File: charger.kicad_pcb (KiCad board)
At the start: 2 copper layers, 3 parts, among them J2 USB_C_Receptacle_PowerOnly_6P

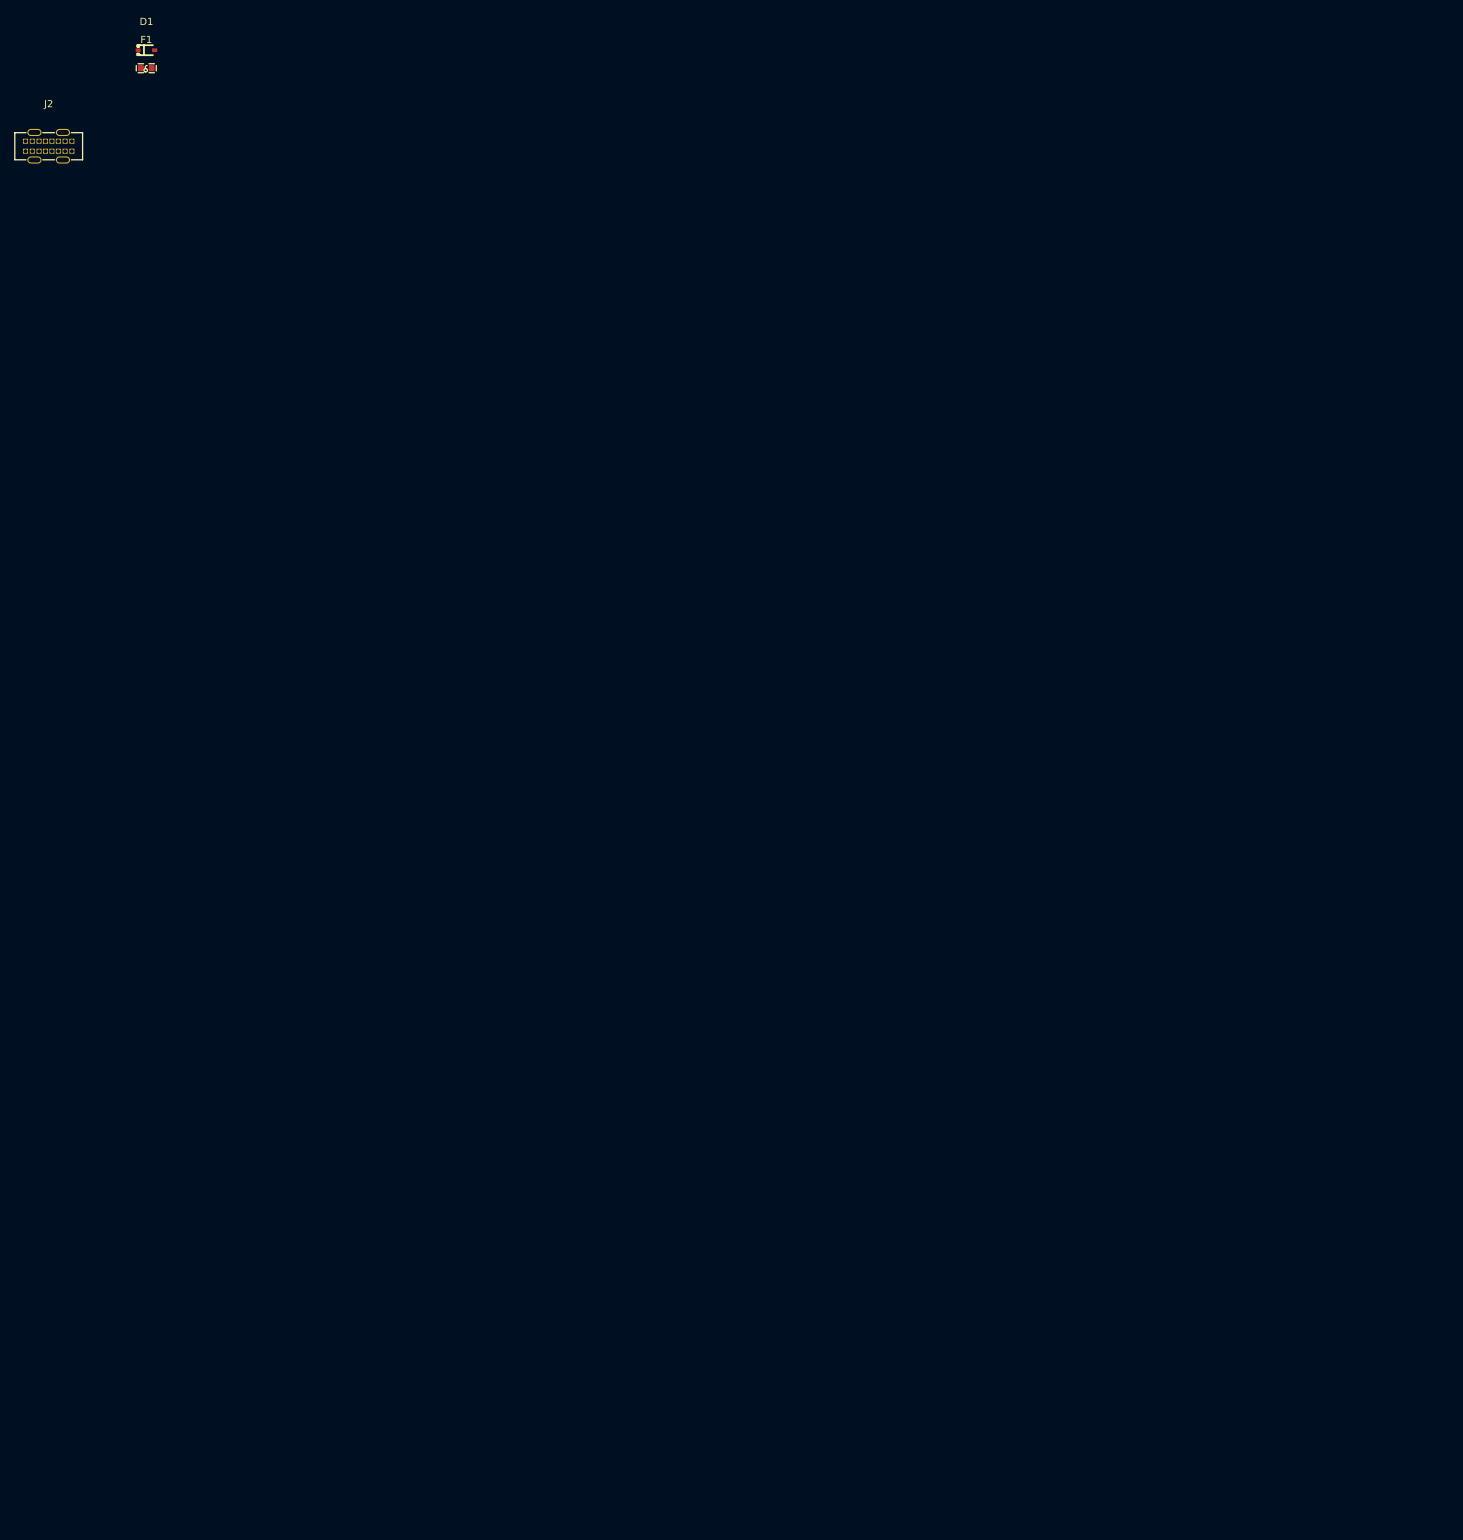
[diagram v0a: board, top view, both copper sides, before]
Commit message: finished getting footprints and started layout
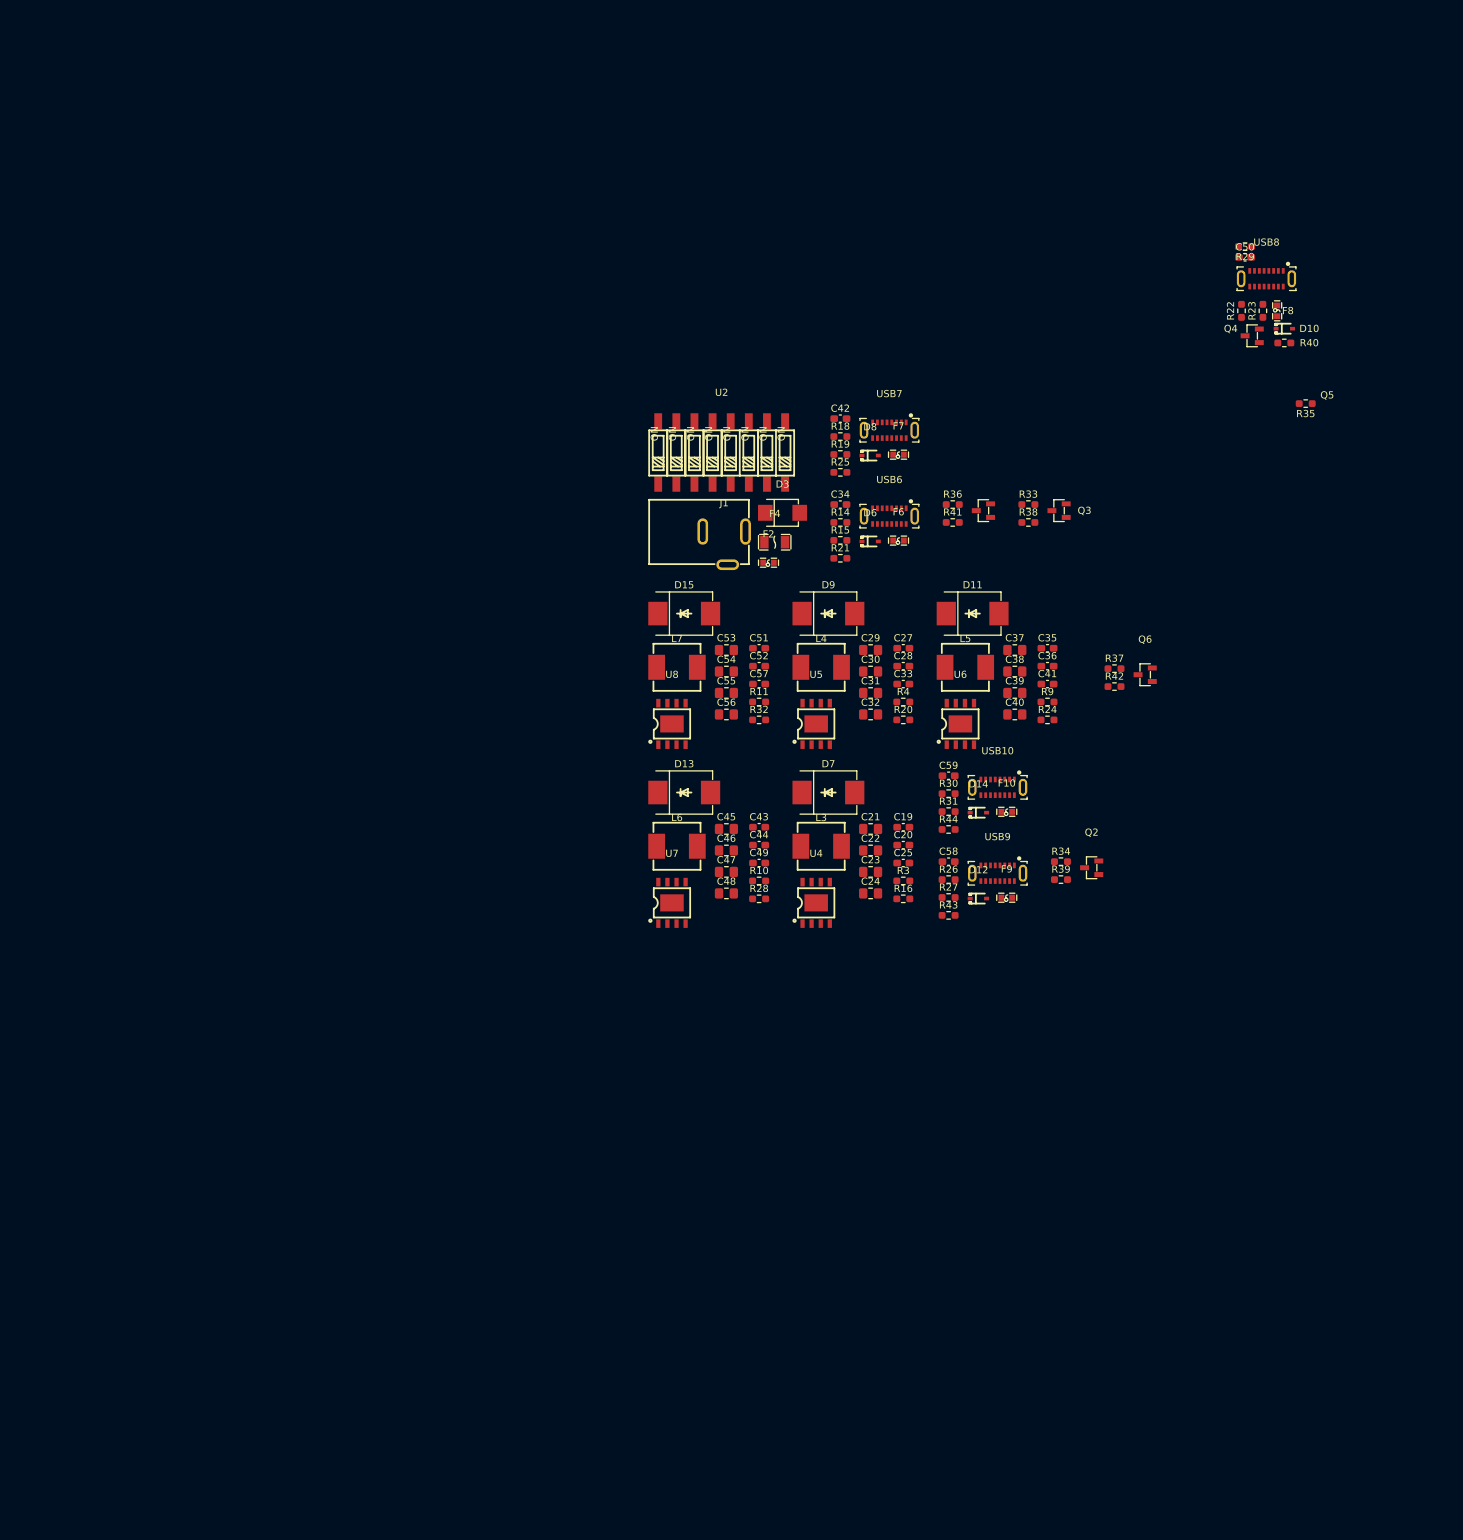
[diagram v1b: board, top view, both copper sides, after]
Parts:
- removed D1: DF2S6P2FU,H3F, easyeda2kicad:USC_L1.7-W1.3-LS2.5-R-RD
- removed F1: Fuse, easyeda2kicad:F0603
- removed J2: USB_C_Receptacle_PowerOnly_6P, easyeda2kicad:TYPE-C-TH_16PLC-H10.0
- added C19: 10nf, Capacitor_SMD:C_0603_1608Metric_Pad1.08x0.95mm_HandSolder, F.Cu at (124.6, 97.9)
- added C20: 0.1uf, Capacitor_SMD:C_0603_1608Metric_Pad1.08x0.95mm_HandSolder, F.Cu at (124.6, 100.4)
- added C21: 10uf, Capacitor_SMD:C_0805_2012Metric_Pad1.18x1.45mm_HandSolder, F.Cu at (120.0, 98.1)
- added C22: 22uF, Capacitor_SMD:C_0805_2012Metric_Pad1.18x1.45mm_HandSolder, F.Cu at (120.0, 101.1)
- added C23: 22uF, Capacitor_SMD:C_0805_2012Metric_Pad1.18x1.45mm_HandSolder, F.Cu at (120.0, 104.1)
- added C24: 10uf, Capacitor_SMD:C_0805_2012Metric_Pad1.18x1.45mm_HandSolder, F.Cu at (120.0, 107.2)
- added C25: 0.1uf, Capacitor_SMD:C_0603_1608Metric_Pad1.08x0.95mm_HandSolder, F.Cu at (124.6, 102.9)
- added C27: 10nf, Capacitor_SMD:C_0603_1608Metric_Pad1.08x0.95mm_HandSolder, F.Cu at (124.6, 72.8)
- added C28: 0.1uf, Capacitor_SMD:C_0603_1608Metric_Pad1.08x0.95mm_HandSolder, F.Cu at (124.6, 75.3)
- added C29: 10uf, Capacitor_SMD:C_0805_2012Metric_Pad1.18x1.45mm_HandSolder, F.Cu at (120.0, 73.0)
- added C30: 22uF, Capacitor_SMD:C_0805_2012Metric_Pad1.18x1.45mm_HandSolder, F.Cu at (120.0, 76.0)
- added C31: 22uF, Capacitor_SMD:C_0805_2012Metric_Pad1.18x1.45mm_HandSolder, F.Cu at (120.0, 79.1)
- added C32: 10uf, Capacitor_SMD:C_0805_2012Metric_Pad1.18x1.45mm_HandSolder, F.Cu at (120.0, 82.1)
- added C33: 0.1uf, Capacitor_SMD:C_0603_1608Metric_Pad1.08x0.95mm_HandSolder, F.Cu at (124.6, 77.8)
- added C34: 4n7, Capacitor_SMD:C_0603_1608Metric_Pad1.08x0.95mm_HandSolder, F.Cu at (115.8, 52.6)
- added C35: 10nf, Capacitor_SMD:C_0603_1608Metric_Pad1.08x0.95mm_HandSolder, F.Cu at (144.8, 72.8)
- added C36: 0.1uf, Capacitor_SMD:C_0603_1608Metric_Pad1.08x0.95mm_HandSolder, F.Cu at (144.8, 75.3)
- added C37: 10uf, Capacitor_SMD:C_0805_2012Metric_Pad1.18x1.45mm_HandSolder, F.Cu at (140.2, 73.0)
- added C38: 22uF, Capacitor_SMD:C_0805_2012Metric_Pad1.18x1.45mm_HandSolder, F.Cu at (140.2, 76.0)
- added C39: 22uF, Capacitor_SMD:C_0805_2012Metric_Pad1.18x1.45mm_HandSolder, F.Cu at (140.2, 79.1)
- added C40: 10uf, Capacitor_SMD:C_0805_2012Metric_Pad1.18x1.45mm_HandSolder, F.Cu at (140.2, 82.1)
- added C41: 0.1uf, Capacitor_SMD:C_0603_1608Metric_Pad1.08x0.95mm_HandSolder, F.Cu at (144.8, 77.8)
- added C42: 4n7, Capacitor_SMD:C_0603_1608Metric_Pad1.08x0.95mm_HandSolder, F.Cu at (115.8, 40.6)
- added C43: 10nf, Capacitor_SMD:C_0603_1608Metric_Pad1.08x0.95mm_HandSolder, F.Cu at (104.4, 97.9)
- added C44: 0.1uf, Capacitor_SMD:C_0603_1608Metric_Pad1.08x0.95mm_HandSolder, F.Cu at (104.4, 100.4)
- added C45: 10uf, Capacitor_SMD:C_0805_2012Metric_Pad1.18x1.45mm_HandSolder, F.Cu at (99.8, 98.1)
- added C46: 22uF, Capacitor_SMD:C_0805_2012Metric_Pad1.18x1.45mm_HandSolder, F.Cu at (99.8, 101.1)
- added C47: 22uF, Capacitor_SMD:C_0805_2012Metric_Pad1.18x1.45mm_HandSolder, F.Cu at (99.8, 104.1)
- added C48: 10uf, Capacitor_SMD:C_0805_2012Metric_Pad1.18x1.45mm_HandSolder, F.Cu at (99.8, 107.2)
- added C49: 0.1uf, Capacitor_SMD:C_0603_1608Metric_Pad1.08x0.95mm_HandSolder, F.Cu at (104.4, 102.9)
- added C50: 4n7, Capacitor_SMD:C_0603_1608Metric_Pad1.08x0.95mm_HandSolder, F.Cu at (172.5, 18.0)
- added C51: 10nf, Capacitor_SMD:C_0603_1608Metric_Pad1.08x0.95mm_HandSolder, F.Cu at (104.4, 72.8)
- added C52: 0.1uf, Capacitor_SMD:C_0603_1608Metric_Pad1.08x0.95mm_HandSolder, F.Cu at (104.4, 75.3)
- added C53: 10uf, Capacitor_SMD:C_0805_2012Metric_Pad1.18x1.45mm_HandSolder, F.Cu at (99.8, 73.0)
- added C54: 22uF, Capacitor_SMD:C_0805_2012Metric_Pad1.18x1.45mm_HandSolder, F.Cu at (99.8, 76.0)
- added C55: 22uF, Capacitor_SMD:C_0805_2012Metric_Pad1.18x1.45mm_HandSolder, F.Cu at (99.8, 79.1)
- added C56: 10uf, Capacitor_SMD:C_0805_2012Metric_Pad1.18x1.45mm_HandSolder, F.Cu at (99.8, 82.1)
- added C57: 0.1uf, Capacitor_SMD:C_0603_1608Metric_Pad1.08x0.95mm_HandSolder, F.Cu at (104.4, 77.8)
- added C58: 4n7, Capacitor_SMD:C_0603_1608Metric_Pad1.08x0.95mm_HandSolder, F.Cu at (130.9, 102.7)
- added C59: 4n7, Capacitor_SMD:C_0603_1608Metric_Pad1.08x0.95mm_HandSolder, F.Cu at (130.9, 90.7)
- added D10: DF2S6P2FU,H3F, easyeda2kicad:USC_L1.7-W1.3-LS2.5-R-RD, F.Cu at (178.0, 28.0)
- added D11: B550C-13-F, easyeda2kicad:SMC_L6.9-W5.9-LS7.9-RD, F.Cu at (134.3, 67.9)
- added D12: DF2S6P2FU,H3F, easyeda2kicad:USC_L1.7-W1.3-LS2.5-R-RD, F.Cu at (135.1, 107.9)
- added D13: B550C-13-F, easyeda2kicad:SMC_L6.9-W5.9-LS7.9-RD, F.Cu at (93.9, 93.0)
- added D14: DF2S6P2FU,H3F, easyeda2kicad:USC_L1.7-W1.3-LS2.5-R-RD, F.Cu at (135.1, 95.8)
- added D15: B550C-13-F, easyeda2kicad:SMC_L6.9-W5.9-LS7.9-RD, F.Cu at (93.9, 67.9)
- added D3: SMBJ5338B, easyeda2kicad:SMB_L4.6-W3.6-LS5.4-RD, F.Cu at (107.7, 53.8)
- added D6: DF2S6P2FU,H3F, easyeda2kicad:USC_L1.7-W1.3-LS2.5-R-RD, F.Cu at (120.0, 57.8)
- added D7: B550C-13-F, easyeda2kicad:SMC_L6.9-W5.9-LS7.9-RD, F.Cu at (114.1, 93.0)
- added D8: DF2S6P2FU,H3F, easyeda2kicad:USC_L1.7-W1.3-LS2.5-R-RD, F.Cu at (120.0, 45.8)
- added D9: B550C-13-F, easyeda2kicad:SMC_L6.9-W5.9-LS7.9-RD, F.Cu at (114.1, 67.9)
- added F10: 0467005.NRHF, easyeda2kicad:F0603, F.Cu at (139.1, 95.7)
- added F2: 0467005.NRHF, easyeda2kicad:F0603, F.Cu at (105.7, 60.8)
- added F4: Littelfuse 0501020.WR, easyeda2kicad:F1206, F.Cu at (106.6, 57.9)
- added F6: 0467005.NRHF, easyeda2kicad:F0603, F.Cu at (123.9, 57.7)
- added F7: 0467005.NRHF, easyeda2kicad:F0603, F.Cu at (123.9, 45.7)
- added F8: 0467005.NRHF, easyeda2kicad:F0603, F.Cu at (177.0, 25.5)
- added F9: 0467005.NRHF, easyeda2kicad:F0603, F.Cu at (139.1, 107.8)
- added J1: XUNPU DC-005-A250, easyeda2kicad:DC-IN-TH_DC-005-A250, F.Cu at (99.5, 58.8)
- added L3: 4.7uH - SHOU HAN CYA0630-4.7UH, easyeda2kicad:IND-SMD_L7.2-W6.6_GPSR07X0, F.Cu at (113.1, 100.5)
- added L4: 4.7uH - SHOU HAN CYA0630-4.7UH, easyeda2kicad:IND-SMD_L7.2-W6.6_GPSR07X0, F.Cu at (113.1, 75.5)
- added L5: 4.7uH - SHOU HAN CYA0630-4.7UH, easyeda2kicad:IND-SMD_L7.2-W6.6_GPSR07X0, F.Cu at (133.3, 75.5)
- added L6: 4.7uH - SHOU HAN CYA0630-4.7UH, easyeda2kicad:IND-SMD_L7.2-W6.6_GPSR07X0, F.Cu at (92.9, 100.5)
- added L7: 4.7uH - SHOU HAN CYA0630-4.7UH, easyeda2kicad:IND-SMD_L7.2-W6.6_GPSR07X0, F.Cu at (92.9, 75.5)
- added Q2: AM2302N-T1-PF-VB, easyeda2kicad:SOT-23-3_L2.9-W1.3-P1.90-LS2.4-BR, F.Cu at (151.0, 103.5)
- added Q3: AM2302N-T1-PF-VB, easyeda2kicad:SOT-23-3_L2.9-W1.3-P1.90-LS2.4-BR, F.Cu at (146.4, 53.5)
- added Q4: AM2302N-T1-PF-VB, easyeda2kicad:SOT-23-3_L2.9-W1.3-P1.90-LS2.4-BR, F.Cu at (173.5, 29.0)
- added Q5: AM2302N-T1-PF-VB, easyeda2kicad:SOT-23-3_L2.9-W1.3-P1.90-LS2.4-BR, F.Cu at (135.8, 53.5)
- added Q6: AM2302N-T1-PF-VB, easyeda2kicad:SOT-23-3_L2.9-W1.3-P1.90-LS2.4-BR, F.Cu at (158.5, 76.5)
- added R10: 31k, Resistor_SMD:R_0603_1608Metric_Pad0.98x0.95mm_HandSolder, F.Cu at (104.4, 105.4)
- added R11: 31k, Resistor_SMD:R_0603_1608Metric_Pad0.98x0.95mm_HandSolder, F.Cu at (104.4, 80.3)
- added R14: 5.1k, Resistor_SMD:R_0603_1608Metric_Pad0.98x0.95mm_HandSolder, F.Cu at (115.8, 55.2)
- added R15: 5.1k, Resistor_SMD:R_0603_1608Metric_Pad0.98x0.95mm_HandSolder, F.Cu at (115.8, 57.7)
- added R16: 10k, Resistor_SMD:R_0603_1608Metric_Pad0.98x0.95mm_HandSolder, F.Cu at (124.6, 107.9)
- added R18: 5.1k, Resistor_SMD:R_0603_1608Metric_Pad0.98x0.95mm_HandSolder, F.Cu at (115.8, 43.1)
- added R19: 5.1k, Resistor_SMD:R_0603_1608Metric_Pad0.98x0.95mm_HandSolder, F.Cu at (115.8, 45.6)
- added R20: 10k, Resistor_SMD:R_0603_1608Metric_Pad0.98x0.95mm_HandSolder, F.Cu at (124.6, 82.8)
- added R21: 1M, Resistor_SMD:R_0603_1608Metric_Pad0.98x0.95mm_HandSolder, F.Cu at (115.8, 60.2)
- added R22: 5.1k, Resistor_SMD:R_0603_1608Metric_Pad0.98x0.95mm_HandSolder, F.Cu at (172.0, 25.5)
- added R23: 5.1k, Resistor_SMD:R_0603_1608Metric_Pad0.98x0.95mm_HandSolder, F.Cu at (175.0, 25.5)
- added R24: 10k, Resistor_SMD:R_0603_1608Metric_Pad0.98x0.95mm_HandSolder, F.Cu at (144.8, 82.8)
- added R25: 1M, Resistor_SMD:R_0603_1608Metric_Pad0.98x0.95mm_HandSolder, F.Cu at (115.8, 48.1)
- added R26: 5.1k, Resistor_SMD:R_0603_1608Metric_Pad0.98x0.95mm_HandSolder, F.Cu at (130.9, 105.2)
- added R27: 5.1k, Resistor_SMD:R_0603_1608Metric_Pad0.98x0.95mm_HandSolder, F.Cu at (130.9, 107.7)
- added R28: 10k, Resistor_SMD:R_0603_1608Metric_Pad0.98x0.95mm_HandSolder, F.Cu at (104.4, 107.9)
- added R29: 1M, Resistor_SMD:R_0603_1608Metric_Pad0.98x0.95mm_HandSolder, F.Cu at (172.5, 16.5)
- added R3: 31k, Resistor_SMD:R_0603_1608Metric_Pad0.98x0.95mm_HandSolder, F.Cu at (124.6, 105.4)
- added R30: 5.1k, Resistor_SMD:R_0603_1608Metric_Pad0.98x0.95mm_HandSolder, F.Cu at (130.9, 93.2)
- added R31: 5.1k, Resistor_SMD:R_0603_1608Metric_Pad0.98x0.95mm_HandSolder, F.Cu at (130.9, 95.7)
- added R32: 10k, Resistor_SMD:R_0603_1608Metric_Pad0.98x0.95mm_HandSolder, F.Cu at (104.4, 82.8)
- added R33: 5.1k, Resistor_SMD:R_0603_1608Metric_Pad0.98x0.95mm_HandSolder, F.Cu at (142.1, 52.6)
- added R34: 5.1k, Resistor_SMD:R_0603_1608Metric_Pad0.98x0.95mm_HandSolder, F.Cu at (146.7, 102.7)
- added R35: 5.1k, Resistor_SMD:R_0603_1608Metric_Pad0.98x0.95mm_HandSolder, F.Cu at (181.0, 38.5)
- added R36: 5.1k, Resistor_SMD:R_0603_1608Metric_Pad0.98x0.95mm_HandSolder, F.Cu at (131.5, 52.6)
- added R37: 5.1k, Resistor_SMD:R_0603_1608Metric_Pad0.98x0.95mm_HandSolder, F.Cu at (154.2, 75.7)
- added R38: 100R, Resistor_SMD:R_0603_1608Metric_Pad0.98x0.95mm_HandSolder, F.Cu at (142.1, 55.2)
- added R39: 100R, Resistor_SMD:R_0603_1608Metric_Pad0.98x0.95mm_HandSolder, F.Cu at (146.7, 105.2)
- added R4: 31k, Resistor_SMD:R_0603_1608Metric_Pad0.98x0.95mm_HandSolder, F.Cu at (124.6, 80.3)
- added R40: 100R, Resistor_SMD:R_0603_1608Metric_Pad0.98x0.95mm_HandSolder, F.Cu at (178.0, 30.0)
- added R41: 100R, Resistor_SMD:R_0603_1608Metric_Pad0.98x0.95mm_HandSolder, F.Cu at (131.5, 55.2)
- added R42: 100R, Resistor_SMD:R_0603_1608Metric_Pad0.98x0.95mm_HandSolder, F.Cu at (154.2, 78.2)
- added R43: 1M, Resistor_SMD:R_0603_1608Metric_Pad0.98x0.95mm_HandSolder, F.Cu at (130.9, 110.2)
- added R44: 1M, Resistor_SMD:R_0603_1608Metric_Pad0.98x0.95mm_HandSolder, F.Cu at (130.9, 98.2)
- added R9: 31k, Resistor_SMD:R_0603_1608Metric_Pad0.98x0.95mm_HandSolder, F.Cu at (144.8, 80.3)
- added U2: DSIC08LSGET_C3293158, easyeda2kicad:SW-SMD_DSIC08LSGET, F.Cu at (99.1, 45.4)
- added U4: EUP3489WIR1, easyeda2kicad:ESOP-8_L4.9-W3.9-P1.27-LS6.0-BL-EP, F.Cu at (112.4, 108.5)
- added U5: EUP3489WIR1, easyeda2kicad:ESOP-8_L4.9-W3.9-P1.27-LS6.0-BL-EP, F.Cu at (112.4, 83.4)
- added U6: EUP3489WIR1, easyeda2kicad:ESOP-8_L4.9-W3.9-P1.27-LS6.0-BL-EP, F.Cu at (132.6, 83.4)
- added U7: EUP3489WIR1, easyeda2kicad:ESOP-8_L4.9-W3.9-P1.27-LS6.0-BL-EP, F.Cu at (92.2, 108.5)
- added U8: EUP3489WIR1, easyeda2kicad:ESOP-8_L4.9-W3.9-P1.27-LS6.0-BL-EP, F.Cu at (92.2, 83.4)
- added USB10: YTC-TC16S-128_C2927282, easyeda2kicad:TYPE-C-SMD_YTC-TC16S-128, F.Cu at (137.8, 92.3)
- added USB6: YTC-TC16S-128_C2927282, easyeda2kicad:TYPE-C-SMD_YTC-TC16S-128, F.Cu at (122.7, 54.3)
- added USB7: YTC-TC16S-128_C2927282, easyeda2kicad:TYPE-C-SMD_YTC-TC16S-128, F.Cu at (122.7, 42.2)
- added USB8: YTC-TC16S-128_C2927282, easyeda2kicad:TYPE-C-SMD_YTC-TC16S-128, F.Cu at (175.5, 21.0)
- added USB9: YTC-TC16S-128_C2927282, easyeda2kicad:TYPE-C-SMD_YTC-TC16S-128, F.Cu at (137.8, 104.3)

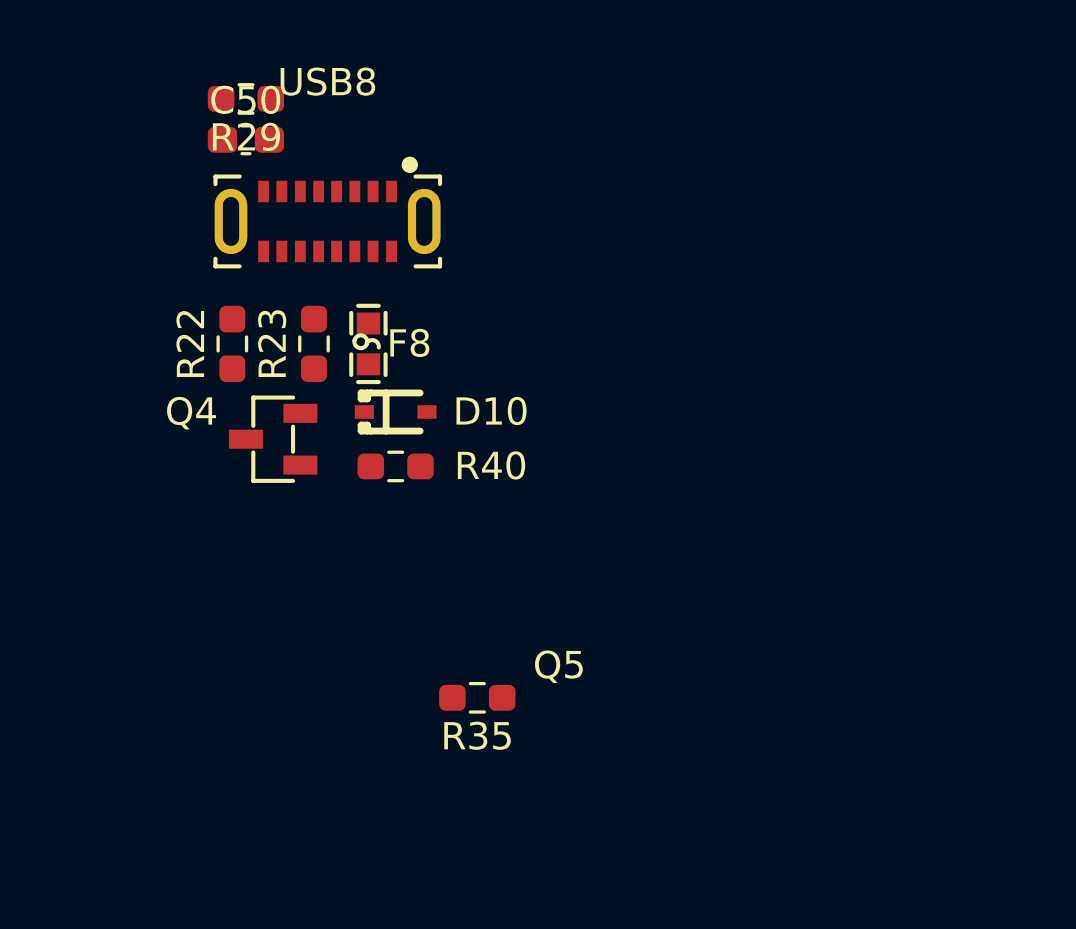
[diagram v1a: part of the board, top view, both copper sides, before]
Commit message: sarted routing of the usb circuitry, almost finished it
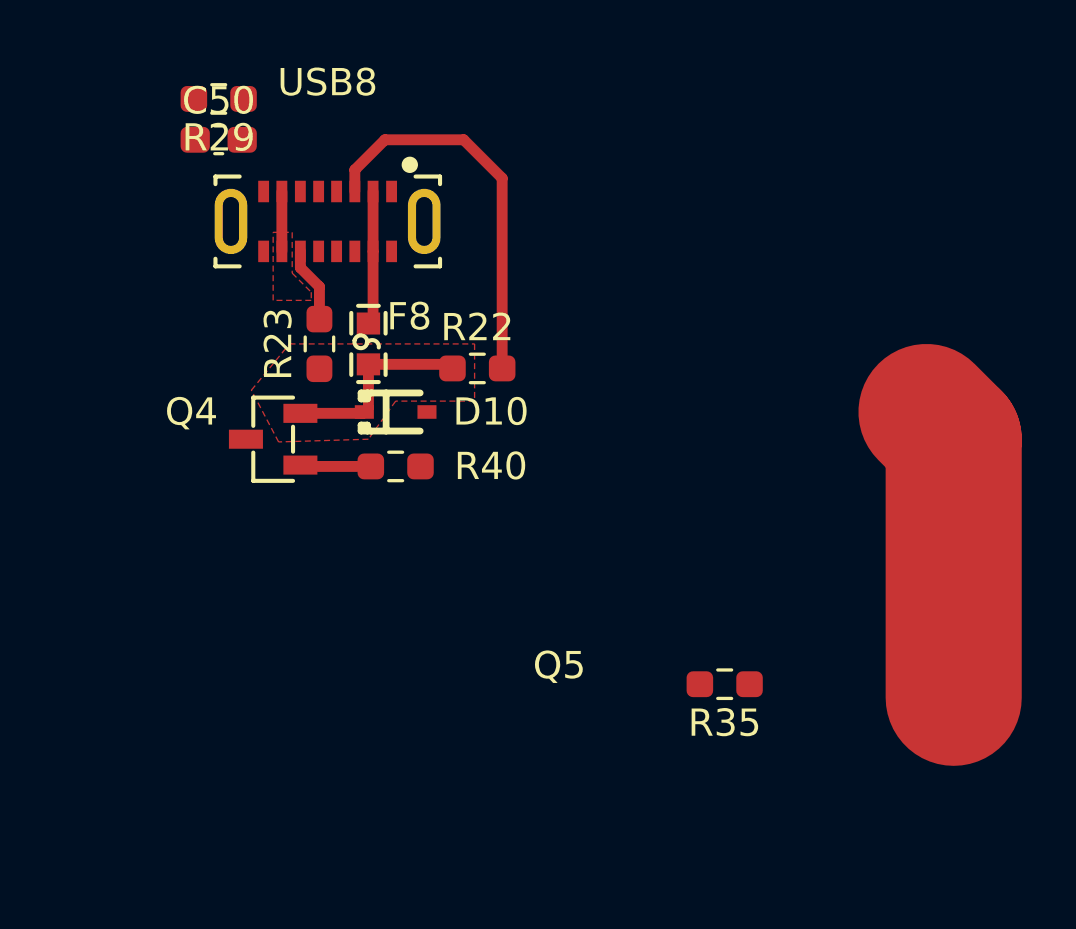
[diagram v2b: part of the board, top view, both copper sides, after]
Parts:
- moved R35 9.10 mm to (190.1, 38.0)
- moved R22 9.04 mm to (181.0, 26.4), turned to 180 degrees
- moved C50 1.00 mm to (171.5, 18.0)
- moved R29 1.00 mm to (171.5, 16.5)
- moved R23 0.20 mm to (175.2, 25.5)
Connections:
- net Net-(F10-Pad1) renamed /REG_USB4/USB receptacle2/Vusb_no_f
- net Net-(F6-Pad1) renamed /REG_USB/USB receptacle2/Vusb_no_f
- net Net-(F7-Pad1) renamed /REG_USB1/USB receptacle2/Vusb_no_f
- net Net-(F8-Pad1) renamed /REG_USB2/USB receptacle2/Vusb_no_f
- net Net-(F9-Pad1) renamed /REG_USB3/USB receptacle2/Vusb_no_f
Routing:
- net Net-(USB8-CC1): track 0.00 -> 13.8 mm
- net (no net): track 0.00 -> 10.9 mm
- net /REG_USB2/USB receptacle2/VBUS: track 0.00 -> 7.54 mm
- net /REG_USB2/USB receptacle2/Vusb_no_f: track 0.00 -> 7.12 mm
- net Net-(USB8-CC2): track 0.00 -> 2.78 mm
- net Net-(Q4-G): track 0.00 -> 2.61 mm
- added copper zone on F.Cu, net /REG_USB2/USB receptacle2/Vusb_no_f
